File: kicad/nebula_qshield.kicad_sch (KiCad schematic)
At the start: 0 parts

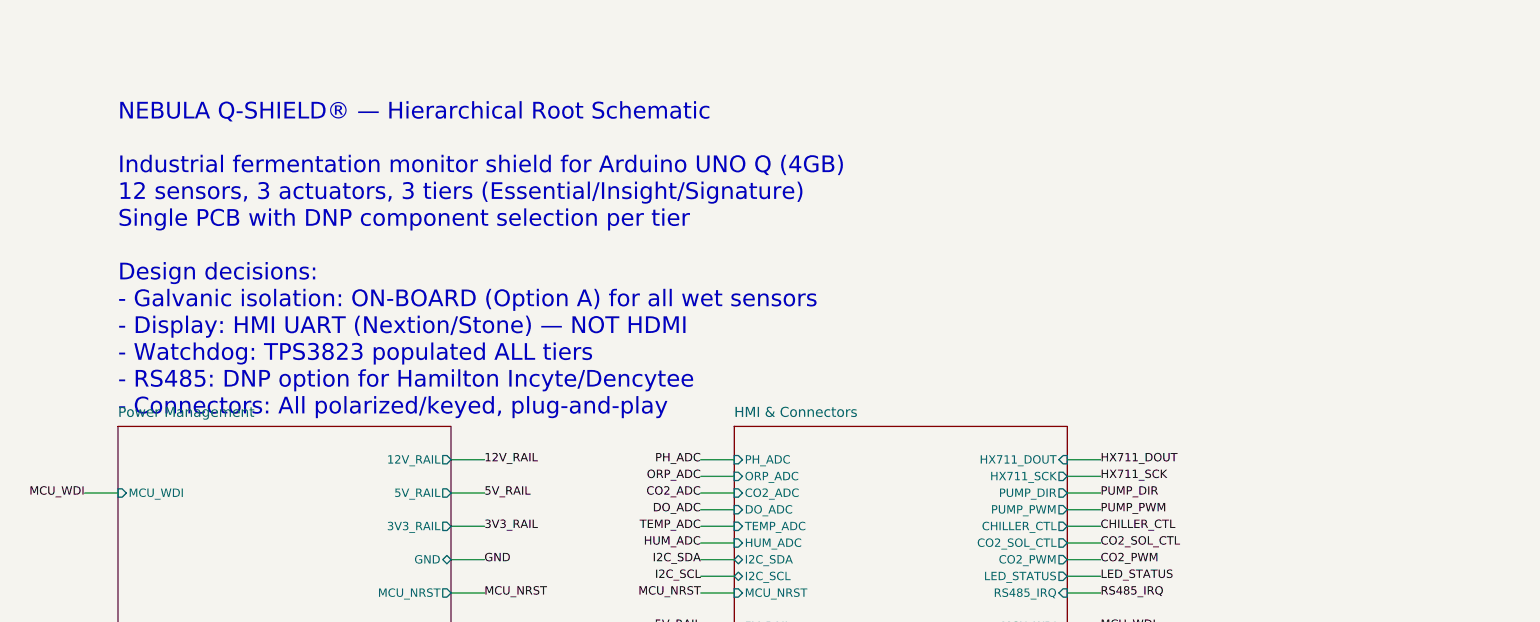
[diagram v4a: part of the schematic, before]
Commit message: feat(sch,pcb,docs): redefine tiers Essential/Insight/Signature and sync DNP
- Tier mapping:
  - Essential: GPS, RTC/timestamp, temperature, pH, ORP
  - Insight: Essential + CO2 pressure (A4), DO (A5), HX711 load cell,
    chiller, recirculation motor, gas solenoid (single gas via K1/J18)
  - Signature: Insight + Hamilton TCD + ACD via RS485 bridge
- Humidity channel (J7/D8/R17/R18/C23) and PWM gas valve (U20/Q5/D14/R28/C27/J22)
  marked DNP in all tiers.
- Update DNP properties in kicad/analog_acquisition.kicad_sch,
  kicad/digital_i2c.kicad_sch, kicad/actuator_drivers.kicad_sch,
  kicad/power_management.kicad_sch using kicad/tier_dnp_mapping.json.
- Update sheet comments and root text block.
- Update docs/04_BOM_PRODUCTION.md section 11, docs/INSIGHT_FABRICATION_ROADMAP.md,
  and docs/DOCUMENTATION_UPDATE_AUDIT.md.
- Add helper tools: build_tier_map.py, apply_tier_dnp4.py, update_tier_comments.py,
  list_actual_components.py, tier_counts.py, validate_sch.py, count_parens.py.
- Sync current PCB state (component positions/nets) to match corrected netlist.

Validation:
- kicad-cli sch erc --severity-all: 0 violaciones
- kicad-cli pcb drc --severity-error: 0 violaciones, 332 unconnected items
- compare_pcb_to_netlist.py: 0 parity problems

Co-Authored-By: Devin AI <158243242+devin-ai-integration[bot]@users.noreply.github.com>
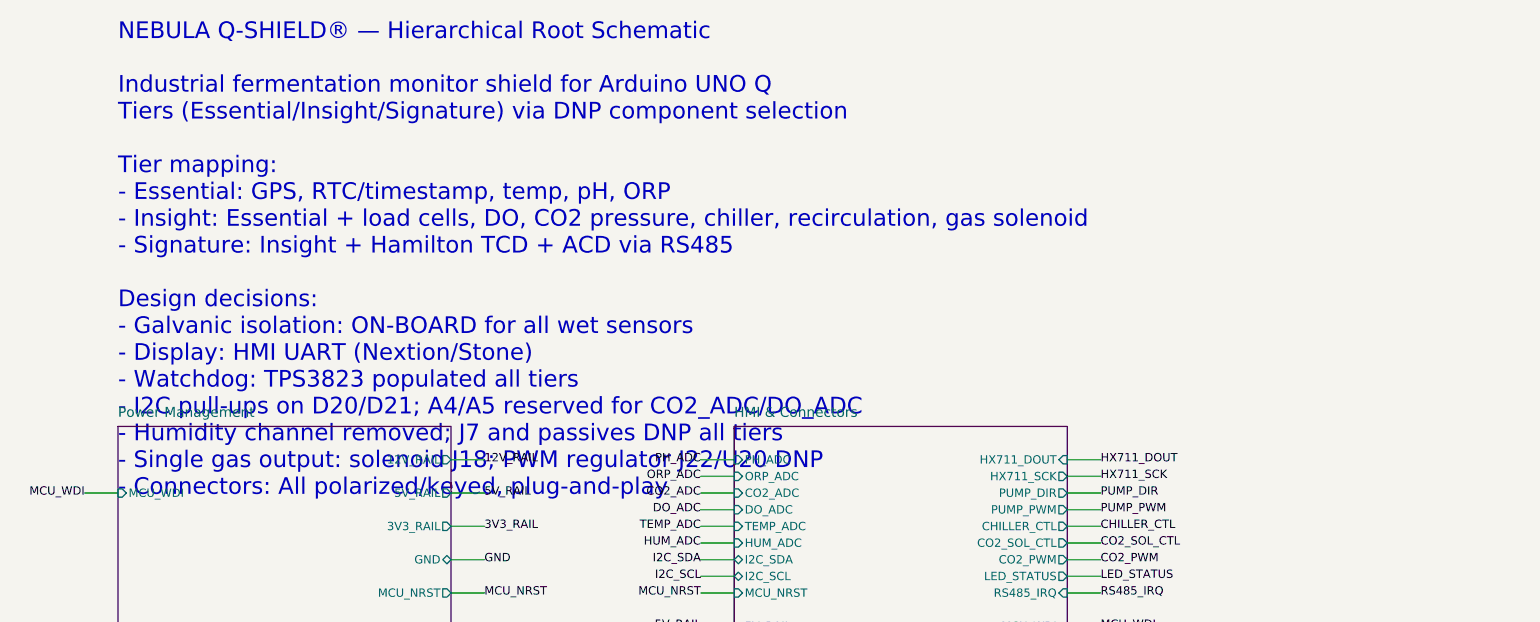
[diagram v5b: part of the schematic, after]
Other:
- note added: "NEBULA Q-SHIELD® — Hierarchical Root Schematic Industrial fermentation monitor shield for Arduino UNO Q Tiers (Essential/Insight/Signature) via DNP component selection Tier mapping: - Essential: GPS, RTC/timestamp, temp, pH, ORP - Insight: Essential + load cells, DO, CO2 pressure, chiller, recirculation, gas solenoid - Signature: Insight + Hamilton TCD + ACD via RS485 Design decisions: - Galvanic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"
- note removed: "NEBULA Q-SHIELD® — Hierarchical Root Schematic Industrial fermentation monitor shield for Arduino UNO Q (4GB) 12 sensors, 3 actuators, 3 tiers (Essential/Insight/Signature) Single PCB with DNP component selection per tier Design decisions: - Galvanic isolation: ON-BOARD (Option A) for all wet sensors - Display: HMI UART (Nextion/Stone) — NOT HDMI - Watchdog: TPS3823 populated ALL tiers - RS485: D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"
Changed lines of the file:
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@@
       (pin "RS485_IRQ" input (at 170.18 76.20 0) (effects (font (size 1.27 1.27)) (justify left)))
   )
-  (text "NEBULA Q-SHIELD® — Hierarchical Root Schematic\n\nIndustrial fermentation monitor shield for Arduino UNO Q (4GB)\n12 sensors, 3 actuators, 3 tiers (Essential/Insight/Signature)\nSingle PCB with DNP component selection per tier\n\nDesign decisions:\n- Galvanic isolation: ON-BOARD (Option A) for all wet sensors\n- Display: HMI UART (Nextion/Stone) — NOT HDMI\n- Watchdog: TPS3823 populated ALL tiers\n- RS485: DNP option for Hamilton Incyte/Dencytee\n- Connectors: All polarized/keyed, plug-and-play"
+  (text "NEBULA Q-SHIELD® — Hierarchical Root Schematic\n\nIndustrial fermentation monitor shield for Arduino UNO Q\nTiers (Essential/Insight/Signature) via DNP component selection\n\nTier mapping:\n- Essential: GPS, RTC/timestamp, temp, pH, ORP\n- Insight: Essential + load cells, DO, CO2 pressure, chiller, recirculation, gas solenoid\n- Signature: Insight + Hamilton TCD + ACD via RS485\n\nDesign decisions:\n- Galvanic isolation: ON-BOARD for all wet sensors\n- Display: HMI UART (Nextion/Stone)\n- Watchdog: TPS3823 populated all tiers\n- I2C pull-ups on D20/D21; A4/A5 reserved for CO2_ADC/DO_ADC\n- Humidity channel removed; J7 and passives DNP all tiers\n- Single gas output: solenoid J18; PWM regulator J22/U20 DNP\n- Connectors: All polarized/keyed, plug-and-play"
     (at 25.4 25.4 0)
     (effects (font (size 2.54 2.54)) (justify left))
